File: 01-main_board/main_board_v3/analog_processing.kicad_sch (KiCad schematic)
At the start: 35 parts, among them IC6 AD7175-8BCPZ-RL7

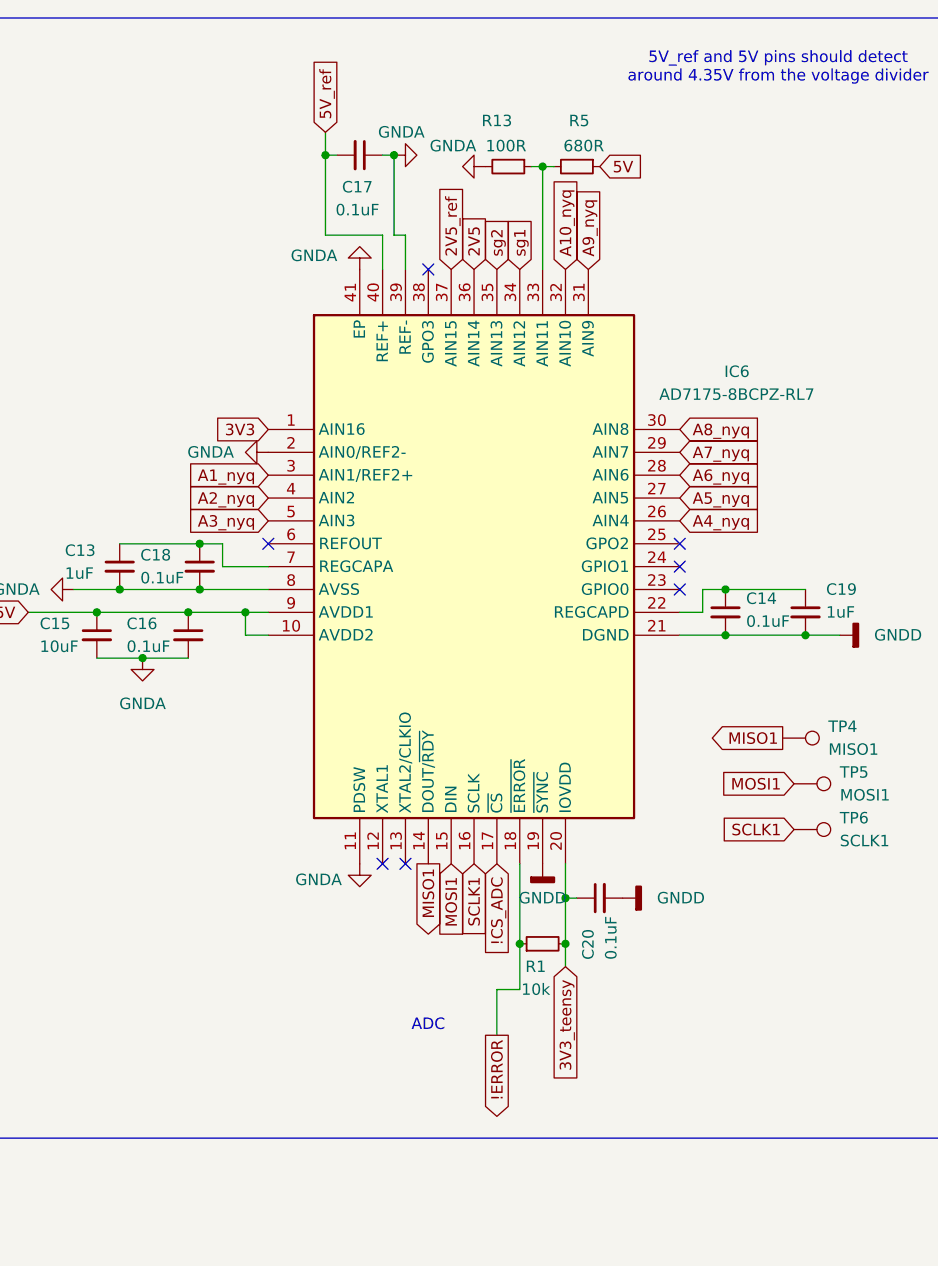
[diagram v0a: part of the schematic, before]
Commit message: arranged layout fully, traces almost done, planes wip
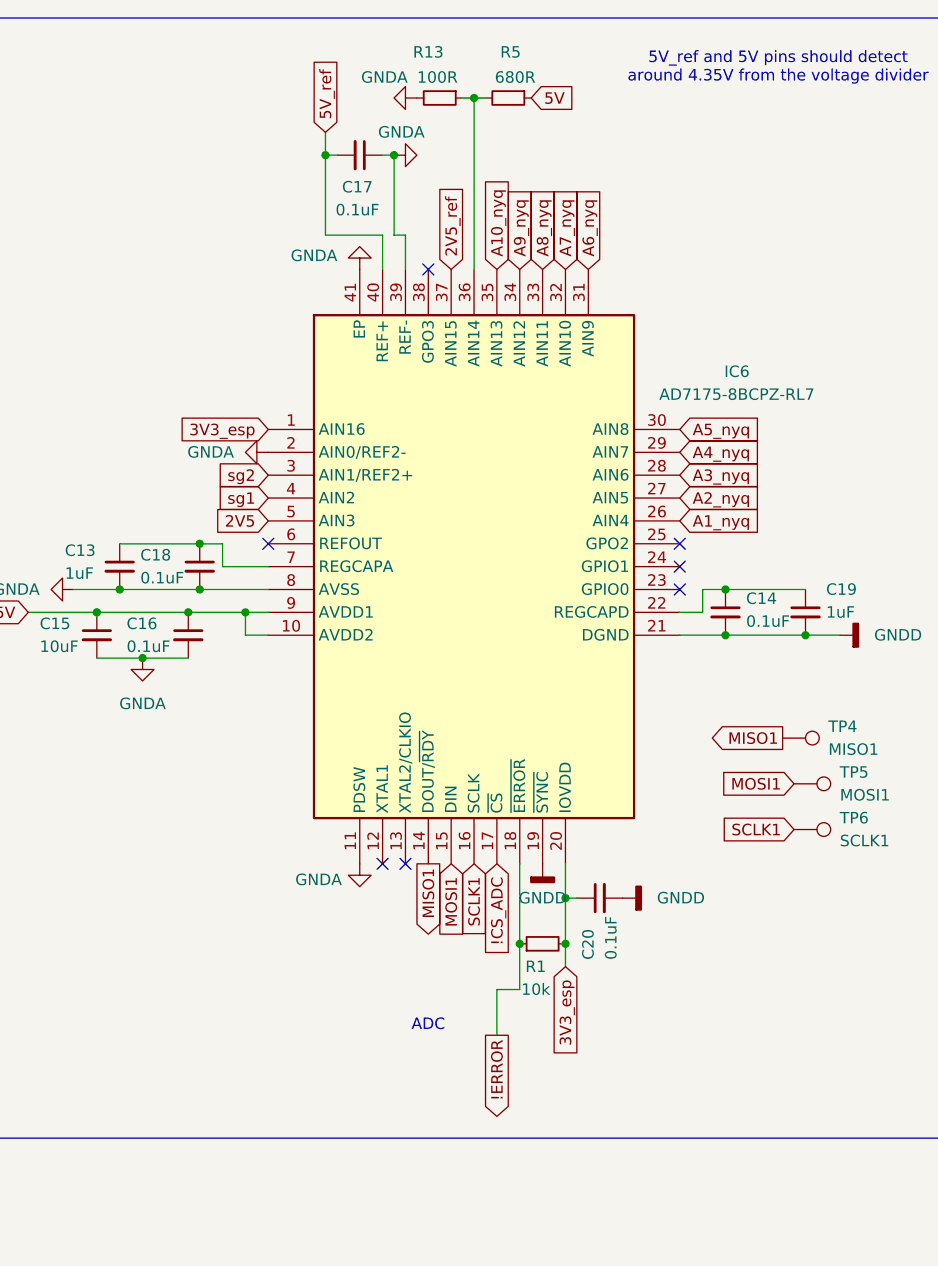
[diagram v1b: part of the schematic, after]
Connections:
- net 3V3_teensy is gone; now on net 3V3_esp: C20.1, IC6.20 (IOVDD), R1.2
- net 2V5: now also IC6.5 (AIN3); no longer IC6.36 (AIN14)
- net A10_nyq: now also IC6.35 (AIN13); no longer IC6.32 (AIN10)
- net A1_nyq: now also IC6.26 (AIN4); no longer IC6.3 (AIN1/REF2+)
- net A2_nyq: now also IC6.27 (AIN5); no longer IC6.4 (AIN2)
- net A3_nyq: now also IC6.28 (AIN6); no longer IC6.5 (AIN3)
- net A4_nyq: now also IC6.29 (AIN7); no longer IC6.26 (AIN4)
- net A5_nyq: now also IC6.30 (AIN8); no longer IC6.27 (AIN5)
- net A6_nyq: now also IC6.31 (AIN9); no longer IC6.28 (AIN6)
- net A7_nyq: now also IC6.32 (AIN10); no longer IC6.29 (AIN7)
- net A8_nyq: now also IC6.33 (AIN11); no longer IC6.30 (AIN8)
- net A9_nyq: now also IC6.34 (AIN12); no longer IC6.31 (AIN9)
- net sg1: now also IC6.4 (AIN2); no longer IC6.34 (AIN12)
- net sg2: now also IC6.3 (AIN1/REF2+); no longer IC6.35 (AIN13)
- net at R13.1, R5.2: now also IC6.36 (AIN14); no longer IC6.33 (AIN11)
- net 3V3 renamed 3V3_esp
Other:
- moved on the sheet: R13, R5

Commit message: finished silkscreen + 3D models
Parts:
- C15: footprint Capacitor_SMD:C_0402_1005Metric -> Capacitor_SMD:C_0603_1608Metric
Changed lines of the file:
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@@
 			)
 		)
-		(property "Footprint" "Capacitor_SMD:C_0402_1005Metric"
+		(property "Footprint" "Capacitor_SMD:C_0603_1608Metric"
 			(at 38.1 97.79 0)
 			(effects

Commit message: Annotated ADC slide
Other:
- note added: "ADC_AIN4"
- note added: "ADC_AIN5"
- note added: "ADC_AIN6"
- note added: "ADC_AIN7"
- note added: "ADC_AIN8"
- note added: "Squid Pinout: - FL: - FR: ADC_AIN6 (AN3) - BL: - BR: ADC_AIN7 (AN4, but this should be AN8..?)"
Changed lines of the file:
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@@
+		)
+	)
+	(text "Squid Pinout:\n- FL:\n- FR: ADC_AIN6 (AN3)\n- BL:\n- BR: ADC_AIN7 (AN4, but this should be AN8..?)"
+		(exclude_from_sim no)
+		(at 165.1 40.132 0)
+		(effects
+			(font
+				(size 1.27 1.27)
+			)
+			(justify left)
+		)
+	)
+	(text "ADC_AIN8"
+		(exclude_from_sim no)
+		(at 190.754 142.494 0)
+		(effects
+			(font
+				(size 1.27 1.27)
+			)
 		)
 	)
@@
 		)
 	)
+	(text "ADC_AIN5"
+		(exclude_from_sim no)
+		(at 191.008 80.772 0)
+		(effects
+			(font
+				(size 1.27 1.27)
+			)
+		)
+	)
+	(text "ADC_AIN7"
+		(exclude_from_sim no)
+		(at 191.008 122.174 0)
+		(effects
+			(font
+				(size 1.27 1.27)
+			)
+		)
+	)
 	(text "5V_ref and 5V pins should detect\naround 4.35V from the voltage divider\n"
 		(exclude_from_sim no)
@@
 		)
 	)
+	(text "ADC_AIN4"
+		(exclude_from_sim no)
+		(at 190.754 59.944 0)
+		(effects
+			(font
+				(size 1.27 1.27)
+			)
+		)
+	)
+	(text "ADC_AIN6"
+		(exclude_from_sim no)
+		(at 191.008 102.108 0)
+		(effects
+			(font
+				(size 1.27 1.27)
+			)
+		)
+	)
